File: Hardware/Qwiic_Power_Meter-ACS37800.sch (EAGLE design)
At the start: 34 parts, among them J2 QWIIC_RIGHT_ANGLE, J4 QWIIC_RIGHT_ANGLE, U1 ACS37800

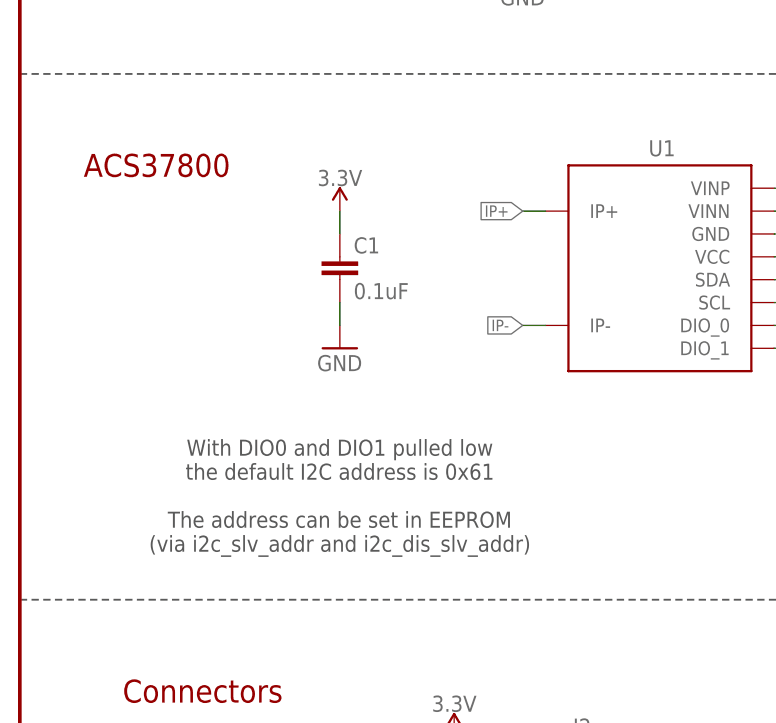
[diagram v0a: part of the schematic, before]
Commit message: Update default I2C address on schematic
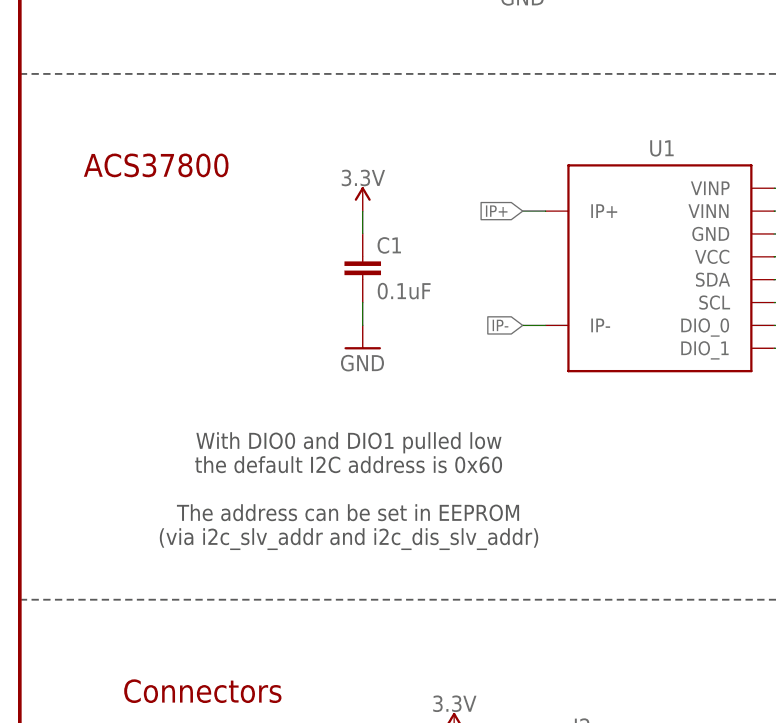
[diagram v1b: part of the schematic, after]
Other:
- note added: "With DIO0 and DIO1 pulled low the default I2C address is 0x60 The address can be set in EEPROM (via i2c_slv_addr and i2c_dis_slv_addr)"
- note removed: "With DIO0 and DIO1 pulled low the default I2C address is 0x61 The address can be set in EEPROM (via i2c_slv_addr and i2c_dis_slv_addr)"
- moved on the sheet: C1
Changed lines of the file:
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@@
 <wire x1="121.92" y1="68.58" x2="121.92" y2="127" width="0.2032" layer="97" style="longdash"/>
 <text x="149.86" y="116.84" size="2.54" layer="94" font="vector" align="center">Voltage Sensing</text>
-<text x="35.56" y="86.36" size="1.778" layer="97" font="vector" align="top-center">With DIO0 and DIO1 pulled low
-the default I2C address is 0x61
+<text x="36.576" y="87.122" size="1.778" layer="97" font="vector" align="top-center">With DIO0 and DIO1 pulled low
+the default I2C address is 0x60
 The address can be set in EEPROM
 (via i2c_slv_addr and i2c_dis_slv_addr)</text>
@@
 <attribute name="NAME" x="182.88" y="152.781" size="1.778" layer="95" font="vector"/>
 </instance>
-<instance part="GND2" gate="1" x="35.56" y="96.52" smashed="yes">
-<attribute name="VALUE" x="33.02" y="93.98" size="1.778" layer="96" font="vector"/>
-</instance>
-<instance part="C1" gate="G$1" x="35.56" y="104.14" smashed="yes">
-<attribute name="NAME" x="37.084" y="107.061" size="1.778" layer="95" font="vector"/>
-<attribute name="VALUE" x="37.084" y="101.981" size="1.778" layer="96" font="vector"/>
-</instance>
-<instance part="SUPPLY3" gate="G$1" x="35.56" y="111.76" smashed="yes">
-<attribute name="VALUE" x="35.56" y="114.554" size="1.778" layer="96" font="vector" align="bottom-center"/>
+<instance part="GND2" gate="1" x="38.1" y="96.52" smashed="yes">
+<attribute name="VALUE" x="35.56" y="93.98" size="1.778" layer="96" font="vector"/>
+</instance>
+<instance part="C1" gate="G$1" x="38.1" y="104.14" smashed="yes">
+<attribute name="NAME" x="39.624" y="107.061" size="1.778" layer="95" font="vector"/>
+<attribute name="VALUE" x="39.624" y="101.981" size="1.778" layer="96" font="vector"/>
+</instance>
+<instance part="SUPPLY3" gate="G$1" x="38.1" y="111.76" smashed="yes">
+<attribute name="VALUE" x="38.1" y="114.554" size="1.778" layer="96" font="vector" align="bottom-center"/>
 </instance>
 <instance part="U$18" gate="G$1" x="213.36" y="53.34" smashed="yes"/>
@@
 <pinref part="C1" gate="G$1" pin="1"/>
 <pinref part="SUPPLY3" gate="G$1" pin="3.3V"/>
-<wire x1="35.56" y1="109.22" x2="35.56" y2="111.76" width="0.1524" layer="91"/>
+<wire x1="38.1" y1="109.22" x2="38.1" y2="111.76" width="0.1524" layer="91"/>
 </segment>
 <segment>
@@
 </segment>
 <segment>
-<wire x1="35.56" y1="101.6" x2="35.56" y2="99.06" width="0.1524" layer="91"/>
+<wire x1="38.1" y1="101.6" x2="38.1" y2="99.06" width="0.1524" layer="91"/>
 <pinref part="GND2" gate="1" pin="GND"/>
 <pinref part="C1" gate="G$1" pin="2"/>
